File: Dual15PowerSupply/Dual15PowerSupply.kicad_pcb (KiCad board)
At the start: 2 copper layers, 100 x 100 mm, 42 parts, among them J1 MKDS 1,5/2-7,62, U1 LT3091xT7, U2 LT3081

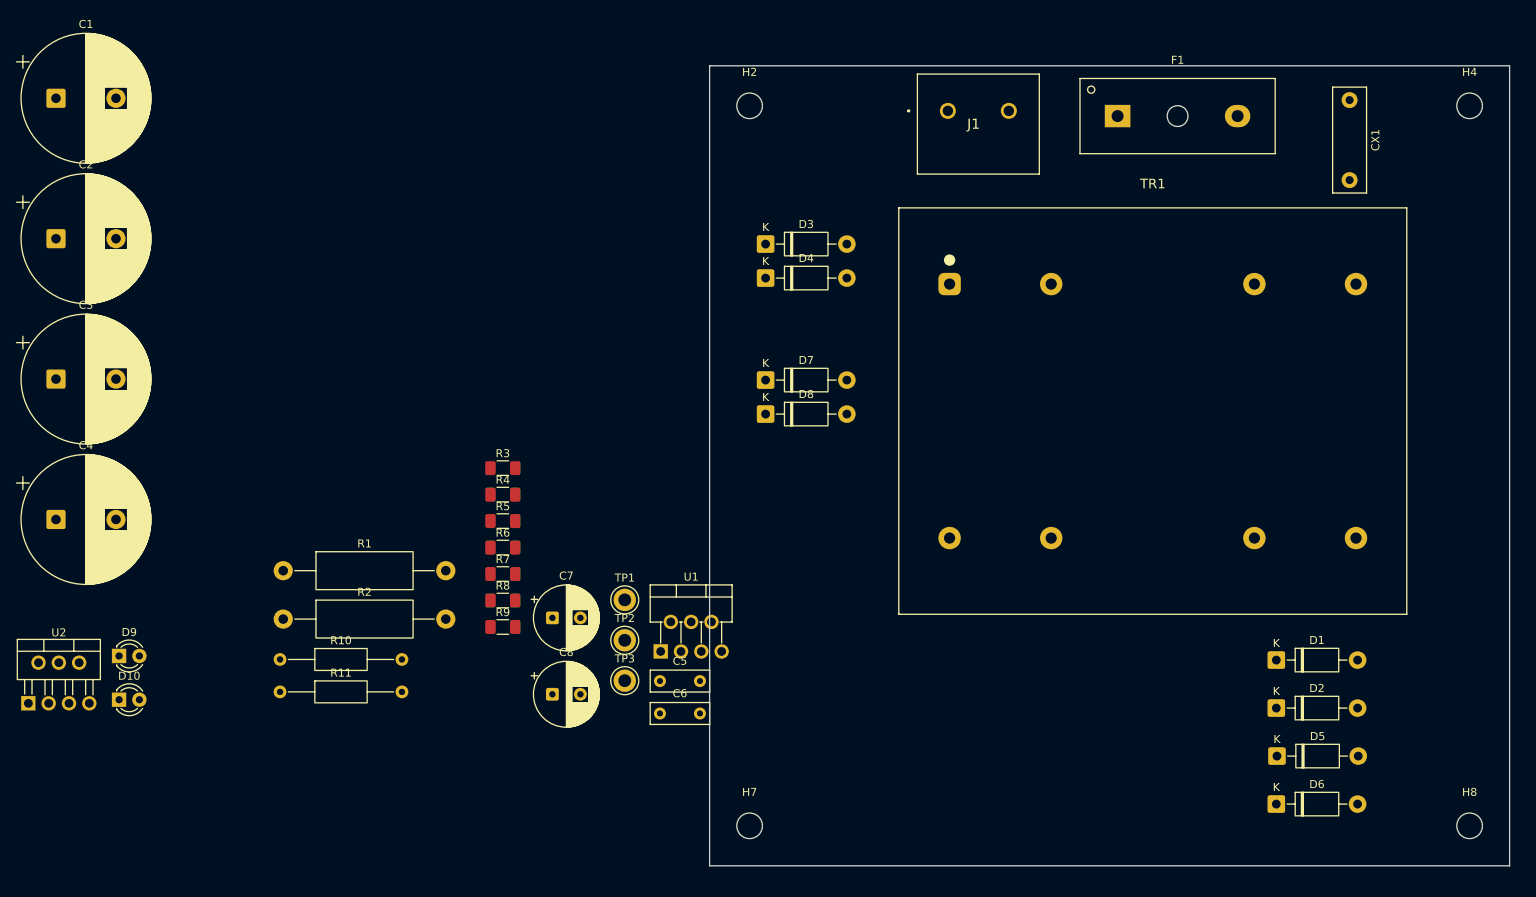
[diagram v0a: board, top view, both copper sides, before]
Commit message: Design rules for creepage
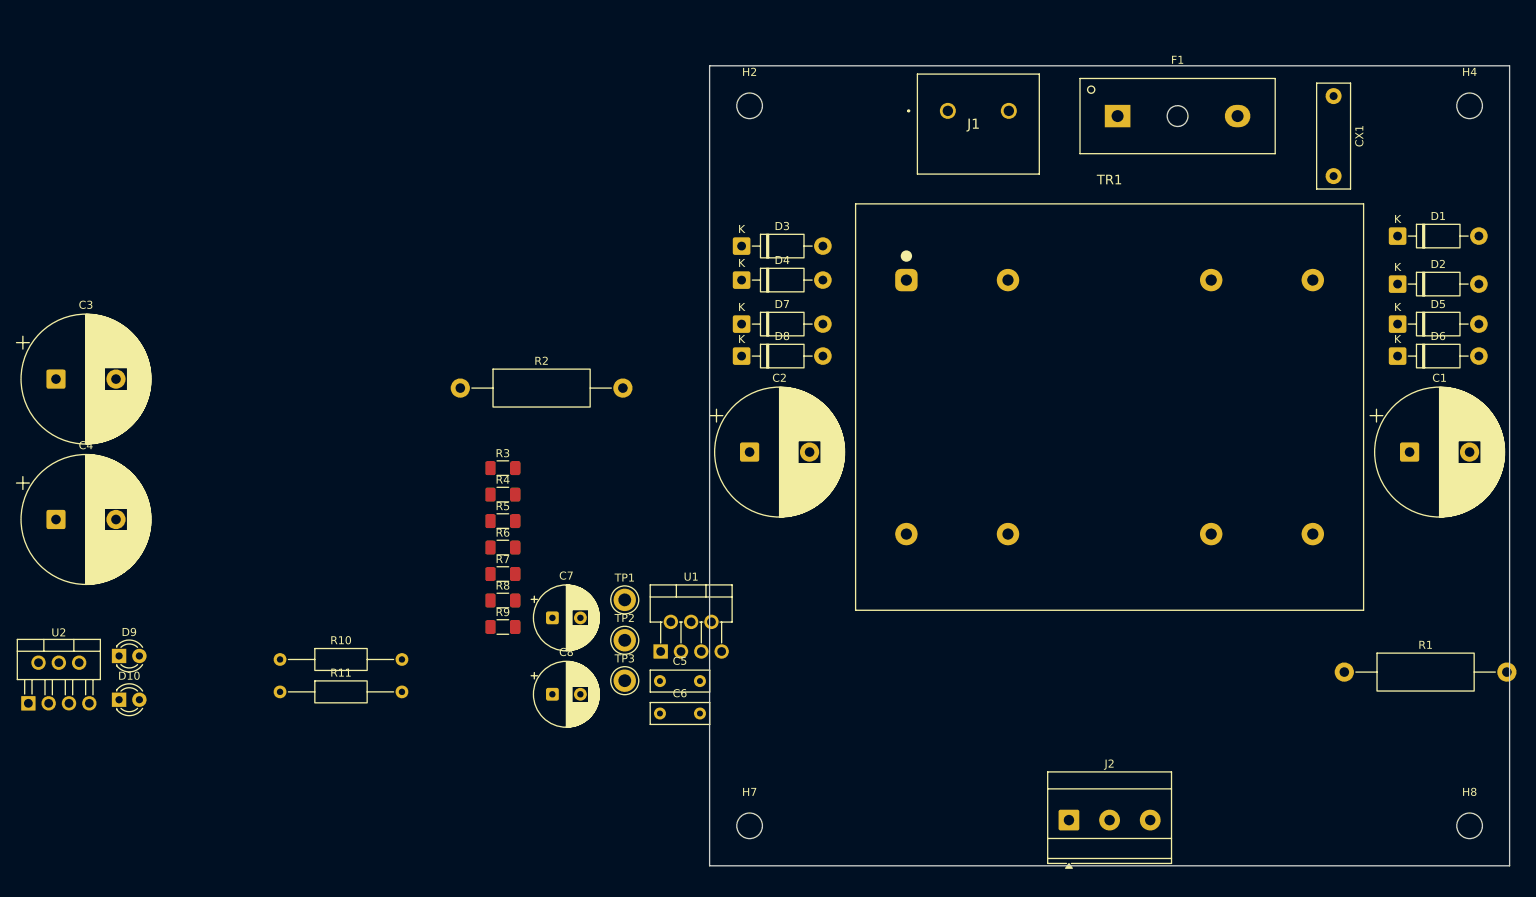
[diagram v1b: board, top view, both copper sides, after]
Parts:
- added J2: +/-15VDC, TerminalBlock_Phoenix:TerminalBlock_Phoenix_MKDS-3-3-5.08_1x03_P5.08mm_Horizontal, F.Cu at (144.9, 126.0)
- F1: value Fuse -> FuseHolder
- J1: value MKDS 1,5/2-7,62 -> 120VAC
- TP3: value 1mV/mA -> -1mV/mA
- moved C1 174.9 mm to (187.5, 80.0)
- moved R1 133.2 mm to (179.3, 107.5)
- moved C2 90.7 mm to (105.0, 80.0)
- moved D6 58.0 mm to (186.0, 68.0)
- moved D5 56.1 mm to (186.0, 64.0)
- moved D1 55.1 mm to (186.0, 53.0)
- moved D2 55.1 mm to (186.0, 59.0)
- moved R2 36.4 mm to (68.8, 72.0)
- moved D8 7.85 mm to (104.0, 68.0)
- moved D7 7.62 mm to (104.0, 64.0)
- moved TR1 5.42 mm to (150.0, 74.4)
- moved D3 3.01 mm to (104.0, 54.2)
- moved D4 3.01 mm to (104.0, 58.5)
- moved CX1 2.06 mm to (178.0, 35.5)
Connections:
- net Net-(D10-K) renamed /-15VDC
- net Net-(D9-A) renamed /+15VDC
- net Net-(U1-IN) renamed /Vin-
- net Net-(U2-IN) renamed /Vin+

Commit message: Layout in work
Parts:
- U1: value LT3091xT7 -> LT3091
- moved C3 177.3 mm to (191.0, 111.0), turned to -90 degrees
- moved U2 162.6 mm to (177.0, 123.0), turned to 180 degrees
- moved D9 136.0 mm to (160.7, 125.5)
- moved R2 122.7 mm to (191.0, 84.0), turned to -90 degrees
- moved D10 111.5 mm to (136.7, 125.5)
- moved C4 95.7 mm to (109.0, 119.0), turned to 90 degrees
- moved C7 76.2 mm to (156.0, 110.0)
- moved R1 70.4 mm to (109.0, 105.0), turned to 90 degrees
- moved C8 61.0 mm to (141.3, 112.0)
- moved U1 41.9 mm to (131.8, 122.8), turned to 180 degrees
- moved C2 10.8 mm to (109.0, 70.0), turned to -90 degrees
- moved J2 10.1 mm to (155.0, 125.5), turned to 180 degrees
- moved D5 6.08 mm to (187.0, 58.0)
- moved D6 6.08 mm to (187.0, 62.0)
- moved D7 6.00 mm to (104.0, 58.0)
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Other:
- board text added: "Dual15 Supply Andrew Fischer 05072026"
- board text removed: "Dual15 Supply Andrew Fischer 03072026"

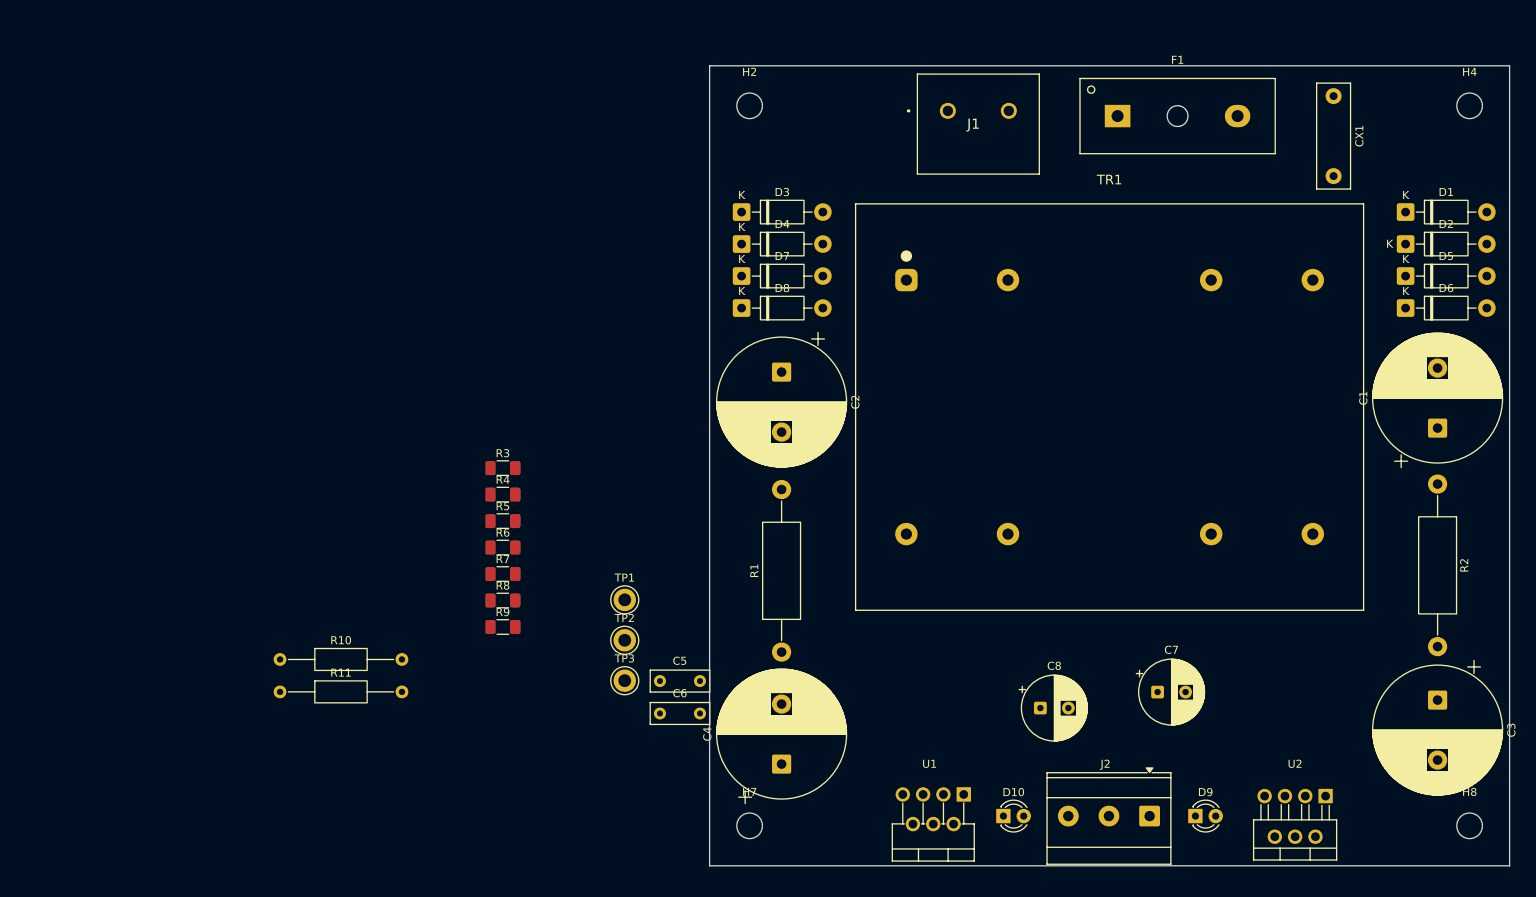
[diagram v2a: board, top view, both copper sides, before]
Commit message: Change to SMD bridge rectifiers
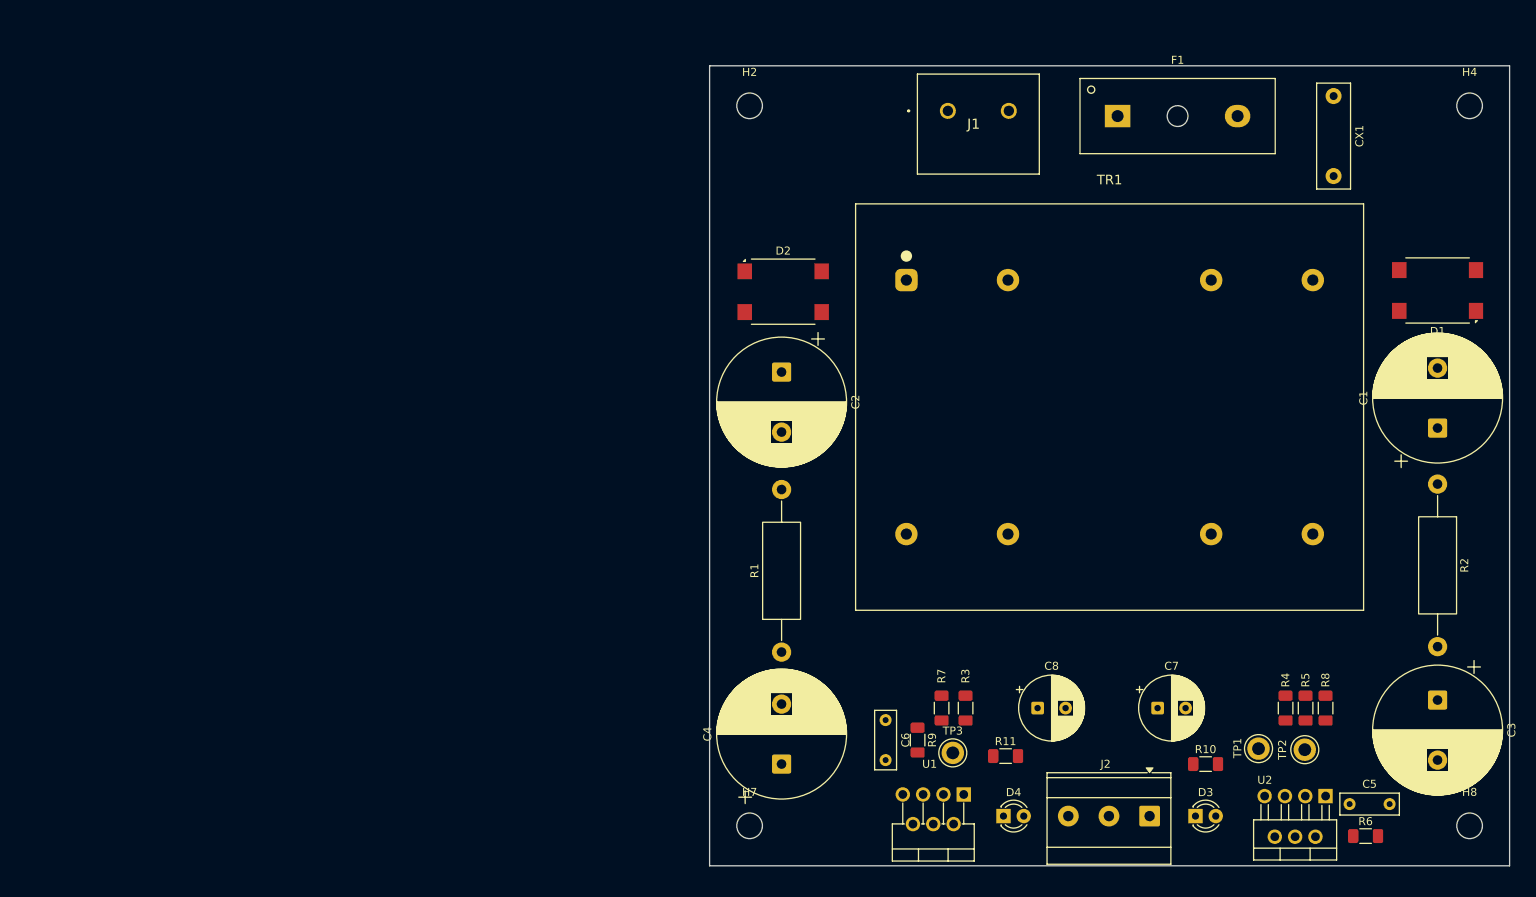
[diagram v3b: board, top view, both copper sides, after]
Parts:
- removed the D3 at (104.0, 50.0)
- removed the D4 at (104.0, 54.0)
- removed D5, D6, D7, D8: UF4007, Diode_THT:D_DO-41_SOD81_P10.16mm_Horizontal
- D1, D2: value UF4007 -> RPMS210; footprint Diode_THT:D_DO-41_SOD81_P10.16mm_Horizontal -> Diode_SMD_Bridge:Diode_Bridge_Panjit_M4_RPMS210
- R10, R11: footprint Resistor_THT:R_Axial_DIN0207_L6.3mm_D2.5mm_P15.24mm_Horizontal -> Resistor_SMD:R_1206_3216Metric_Pad1.30x1.75mm_HandSolder
- moved R10 116.4 mm to (162.0, 119.0)
- moved R6 113.7 mm to (182.0, 128.0)
- moved R8 103.7 mm to (177.0, 112.0), turned to -90 degrees
- moved R5 103.0 mm to (174.5, 112.0), turned to 90 degrees
- moved R4 101.4 mm to (172.0, 112.0), turned to 90 degrees
- moved R11 91.0 mm to (137.0, 118.0)
- moved C5 87.6 mm to (180.0, 124.0)
- moved TP2 86.1 mm to (174.4, 117.2)
- moved TP1 81.4 mm to (168.6, 117.1)
- moved D2 78.0 mm to (109.2, 60.0)
- moved R3 65.2 mm to (132.0, 112.0), turned to -90 degrees
- moved R7 57.3 mm to (129.0, 112.0), turned to -90 degrees
- moved R9 53.7 mm to (126.0, 116.0), turned to -90 degrees
- moved TP3 42.0 mm to (130.4, 117.6)
- moved C6 28.2 mm to (122.0, 113.5), turned to -90 degrees
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- renumbered D9 to D3, D10 to D4
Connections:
- C2 pad 2: Net-(D4-A) (its old number) -> Net-(D2--)
- D1 pad 2: Net-(D1-A) -> GND
- D2 pad 1: Net-(D1-A) -> GND
- D2 pad 2: GND -> Net-(D2--)
- R1 pad 2: Net-(D4-A) (its old number) -> Net-(D2--)
- TR1 pad 5: Net-(D3-A) -> Net-(D2-Pad3)
- TR1 pad 6: Net-(D7-A) -> Net-(D2-Pad4)
- TR1 pad 7: Net-(D1-A) -> Net-(D1-Pad3)
- TR1 pad 8: Net-(D5-A) -> Net-(D1-Pad4)

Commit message: Layout in progress
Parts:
- C1, C2: value 2200µF -> 1000µF; footprint Capacitor_THT:CP_Radial_D16.0mm_P7.50mm -> Capacitor_THT:CP_Radial_D12.5mm_P5.00mm
- C3, C4: footprint Capacitor_THT:CP_Radial_D16.0mm_P7.50mm -> Capacitor_THT:CP_Radial_D12.5mm_P5.00mm
- F1: footprint Fuseholder_Wurth:Wurth_WR-FSH_696105003002 -> Fuseholder_Wurth_WR-FSH:J_Wurth_WR-FSH_696105003002
- J1: footprint TerminalBlock_762:MKDS 5_2-7,62 -> TerminalBlock_Phoenix:PHOENIX_1731721
- U2: footprint Package_TO_SOT_THT:TO-220-7_P2.54x5.08mm_StaggerOdd_Lead3.08mm_Vertical -> Package_TO_SOT_THT:TO-220-7_P2.54x3.7mm_StaggerOdd_Lead3.8mm_Vertical
- moved R6 21.4 mm to (168.4, 111.5), turned to 180 degrees
- moved C5 20.6 mm to (170.0, 106.0), turned to 180 degrees
- moved TP1 14.0 mm to (182.0, 121.0)
- moved R5 13.6 mm to (176.0, 125.5), turned to -90 degrees
- moved F1 13.5 mm to (145.0, 38.5)
- moved TP2 12.4 mm to (182.0, 127.0), turned to -90 degrees
- moved R4 10.3 mm to (178.5, 120.0), turned to -90 degrees
- moved J2 10.1 mm to (144.9, 126.0), turned to 0 degrees
- moved R8 8.73 mm to (173.5, 120.0), turned to 90 degrees
- moved U2 8.73 mm to (173.5, 115.0), turned to 0 degrees
- moved R10 8.51 mm to (167.5, 125.5)
- moved J1 7.47 mm to (135.0, 32.0), turned to 180 degrees
- moved C4 4.00 mm to (109.0, 115.0), turned to 0 degrees
- moved C7 3.64 mm to (155.0, 115.5), turned to 90 degrees
- moved CX1 3.61 mm to (180.0, 38.5), turned to 180 degrees
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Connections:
- net Net-(D1-+) renamed /RawDC+
- net Net-(D1-Pad3) renamed /S1
- net Net-(D1-Pad4) renamed /S2
- net Net-(D2--) renamed /RawDC-
- net Net-(D2-Pad3) renamed /S4
- net Net-(D2-Pad4) renamed /S3
- J1 pad 1: /AC_N -> /AC_L
- J1 pad 2: /AC_L -> /AC_N
- J2 pad 1: /+15VDC -> /-15VDC
- J2 pad 3: /-15VDC -> /+15VDC
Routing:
- net /AC_L_Fused: track 0.00 -> 85.6 mm
- net /AC_N: track 0.00 -> 70.6 mm
- net /S3: track 0.00 -> 39.8 mm
- net /S1: track 0.00 -> 35.2 mm
- net /S2: track 0.00 -> 35.2 mm, vias 0 -> 1
- net /S4: track 0.00 -> 29.3 mm
- net /RawDC-: track 0.00 -> 24.7 mm
- net /RawDC+: track 0.00 -> 24.5 mm
- net GND: track 0.00 -> 17.3 mm
- net /Vin+: track 0.00 -> 17.1 mm
- net /AC_L: track 0.00 -> 14.3 mm
- net /Vin-: track 0.00 -> 11.4 mm
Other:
- board text added: "L"
- board text added: "N"

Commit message: layout
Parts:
- R4: footprint Resistor_SMD:R_1206_3216Metric_Pad1.30x1.75mm_HandSolder -> Resistor_SMD:R_0805_2012Metric_Pad1.20x1.40mm_HandSolder
- moved R5 5.50 mm to (176.0, 120.0)
- moved TP1 1.00 mm to (183.0, 121.0)
- moved R4 0.09 mm to (178.6, 120.0)
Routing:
- net Net-(U2-TEMP): track 0.00 -> 4.00 mm
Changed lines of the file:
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@@
 	(footprint "TestPoint:TestPoint_Keystone_5005-5009_Compact"
 		(layer "F.Cu")
-		(at 182 121)
+		(at 183 121)
 		(descr "Keystone THM Compact Test Point 5005-5009, http://www.keyelco.com/product-pdf.cfm?p=1314")
 		(tags "Through Hole Mount Test Points")
@@
 	(footprint "Resistor_SMD:R_1206_3216Metric_Pad1.30x1.75mm_HandSolder"
 		(layer "F.Cu")
-		(at 176 125.5 -90)
+		(at 176 120 -90)
 		(descr "Resistor SMD 1206 (3216 Metric), square (rectangular) end terminal, IPC-7351 nominal with elongated pad for handsoldering. (Body size source: IPC-SM-782 page 72, https://www.pcb-3d.com/wordpress/wp-content/uploads/ipc-sm-782a_amendment_1_and_2.pdf)")
 		(tags "resistor handsolder")
@@
 		)
 		(property "Value" "4.99K"
-			(at 0 4.5 90)
+			(at 7 0 90)
 			(layer "F.Fab")
 			(effects
@@
 		)
 		(property "Value" "LT3081"
-			(at 3.81 2.15 0)
+			(at 7.9 -9.3 0)
 			(layer "F.Fab")
 			(effects
@@
 		)
 	)
-	(footprint "Resistor_SMD:R_1206_3216Metric_Pad1.30x1.75mm_HandSolder"
+	(footprint "Resistor_SMD:R_0805_2012Metric_Pad1.20x1.40mm_HandSolder"
 		(layer "F.Cu")
-		(at 178.5 119.95 -90)
-		(descr "Resistor SMD 1206 (3216 Metric), square (rectangular) end terminal, IPC-7351 nominal with elongated pad for handsoldering. (Body size source: IPC-SM-782 page 72, https://www.pcb-3d.com/wordpress/wp-content/uploads/ipc-sm-782a_amendment_1_and_2.pdf)")
+		(at 178.58 120 -90)
+		(descr "Resistor SMD 0805 (2012 Metric), square (rectangular) end terminal, IPC-7351 nominal with elongated pad for handsoldering. (Body size source: IPC-SM-782 page 72, https://www.pcb-3d.com/wordpress/wp-content/uploads/ipc-sm-782a_amendment_1_and_2.pdf)")
 		(tags "resistor handsolder")
 		(property "Reference" "R4"
-			(at 3.5 0 90)
+			(at 0 -1.65 90)
 			(layer "F.SilkS")
 			(effects
@@
 		)
 		(property "Value" "1K"
-			(at 0 -2 90)
+			(at 3.05 0 90)
 			(layer "F.Fab")
 			(effects
@@
 			)
 		)
-		(property "MPN" "RC1206FR-101KL "
+		(property "MPN" "RT0805FRE071KL"
 			(at 0 0 270)
 			(unlocked yes)
@@
 			)
 		)
-		(property "Mouser" "603-RC1206FR-101KL "
+		(property "Mouser" "603-RT0805FRE071KL "
 			(at 0 0 270)
 			(unlocked yes)
@@
 		(duplicate_pad_numbers_are_jumpers no)
 		(fp_line
-			(start -0.727064 0.91)
-			(end 0.727064 0.91)
+			(start -0.227064 0.735)
+			(end 0.227064 0.735)
 			(stroke
 				(width 0.12)
@@
 		)
 		(fp_line
-			(start -0.727064 -0.91)
-			(end 0.727064 -0.91)
+			(start -0.227064 -0.735)
+			(end 0.227064 -0.735)
 			(stroke
 				(width 0.12)
@@
 		)
 		(fp_rect
-			(start -2.45 -1.13)
-			(end 2.45 1.13)
+			(start -1.85 -0.95)
+			(end 1.85 0.95)
 			(stroke
 				(width 0.05)
@@
 		)
 		(fp_rect
-			(start -1.6 -0.8)
-			(end 1.6 0.8)
+			(start -1 -0.625)
+			(end 1 0.625)
 			(stroke
 				(width 0.1)
@@
 			(effects
 				(font
-					(size 0.8 0.8)
-					(thickness 0.12)
+					(size 0.5 0.5)
+					(thickness 0.08)
 				)
 			)
 		)
 		(pad "1" smd roundrect
-			(at -1.55 0 270)
-			(size 1.3 1.75)
+			(at -1 0 270)
+			(size 1.2 1.4)
 			(layers "F.Cu" "F.Mask" "F.Paste")
-			(roundrect_rratio 0.192308)
+			(roundrect_rratio 0.208333)
 			(net "Net-(U2-TEMP)")
 			(pintype "passive")
 		)
 		(pad "2" smd roundrect
-			(at 1.55 0 270)
-			(size 1.3 1.75)
+			(at 1 0 270)
+			(size 1.2 1.4)
 			(layers "F.Cu" "F.Mask" "F.Paste")
-			(roundrect_rratio 0.192308)
+			(roundrect_rratio 0.208333)
 			(net "GND")
 			(pintype "passive")
 		)
 		(embedded_fonts no)
-		(model "${KICAD10_3DMODEL_DIR}/Resistor_SMD.3dshapes/R_1206_3216Metric.step"
+		(model "${KICAD10_3DMODEL_DIR}/Resistor_SMD.3dshapes/R_0805_2012Metric.step"
 			(offset
 				(xyz 0 0 0)
@@
 	)
 	(segment
+		(start 178.58 115)
+		(end 178.58 119)
+		(width 1)
+		(layer "F.Cu")
+		(net "Net-(U2-TEMP)")
+	)
+	(segment
